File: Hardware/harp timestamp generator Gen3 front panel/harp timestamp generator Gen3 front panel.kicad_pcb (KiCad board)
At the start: 2 copper layers, 133 x 35 mm, 12 parts

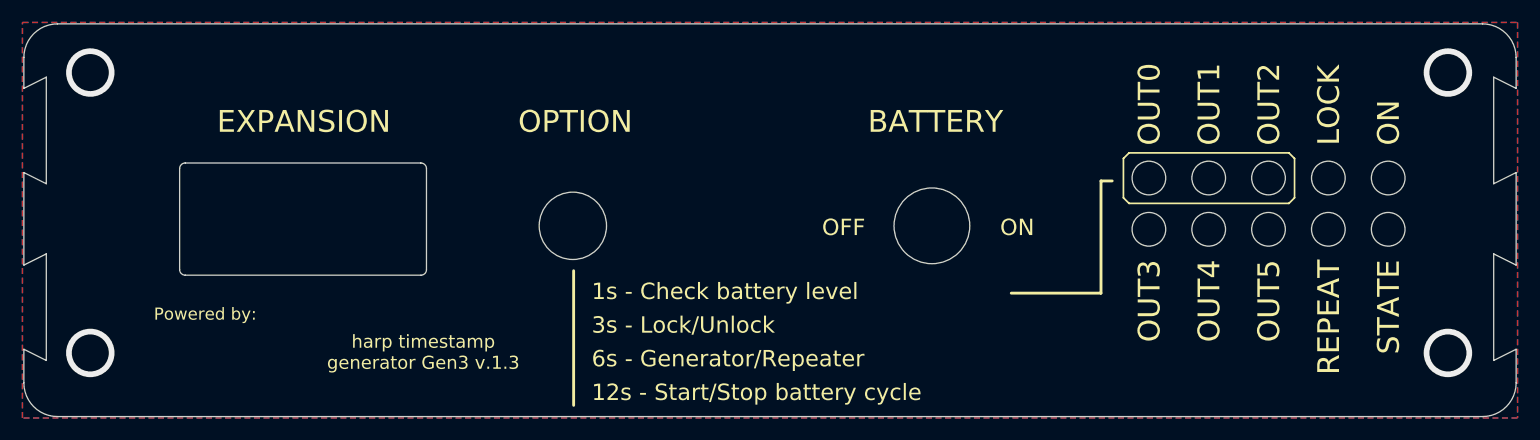
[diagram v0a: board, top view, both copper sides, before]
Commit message: ajuste posição ficha USB-C
> ajuste posição ficha USB-C
. actualizados manufacturing files:
   Gerbers & Drills & .d356 & P&P
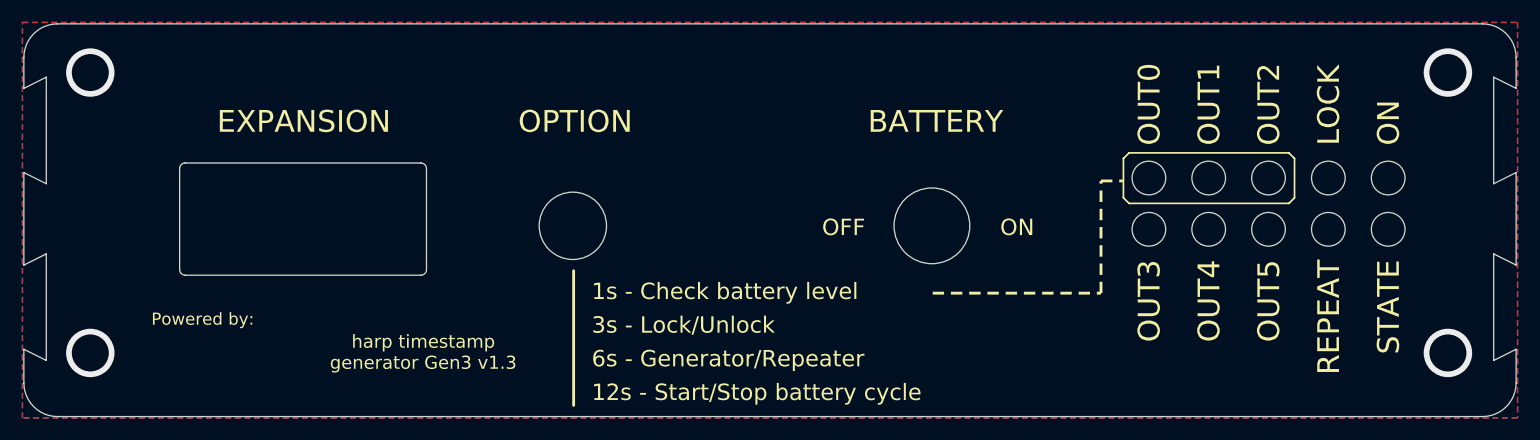
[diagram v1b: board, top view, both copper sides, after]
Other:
- board text added: "harp timestamp generator Gen3 v1.3"
- board text removed: "harp timestamp generator Gen3 v.1.3"
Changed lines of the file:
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@@
 			(usegerberattributes yes)
 			(usegerberadvancedattributes yes)
-			(creategerberjobfile yes)
+			(creategerberjobfile no)
 			(dashed_line_dash_ratio 12)
 			(dashed_line_gap_ratio 3)
@@
 			(plotframeref no)
 			(mode 1)
-			(useauxorigin no)
+			(useauxorigin yes)
 			(pdf_front_fp_property_popups yes)
 			(pdf_back_fp_property_popups yes)
@@
 			(sketchdnponfab yes)
 			(crossoutdnponfab yes)
-			(subtractmaskfromsilk no)
+			(subtractmaskfromsilk yes)
 			(outputformat 1)
 			(mirror no)
-			(drillshape 1)
+			(drillshape 0)
 			(scaleselection 1)
-			(outputdirectory "")
+			(outputdirectory "manufacturing/gerbers/")
 		)
 	)
@@
 	)
 	(gr_line
-		(start 170.0011 111.5036)
+		(start 163.0011 111.5036)
 		(end 178.0011 111.5036)
 		(stroke
 			(width 0.254)
-			(type solid)
+			(type dash)
 		)
 		(layer "F.SilkS")
@@
 	(gr_line
 		(start 178.0011 101.5036)
-		(end 179.0011 101.5036)
+		(end 179.95 101.5036)
 		(stroke
 			(width 0.254)
-			(type solid)
+			(type dash)
 		)
 		(layer "F.SilkS")
@@
 		(stroke
 			(width 0.254)
-			(type solid)
+			(type dash)
 		)
 		(layer "F.SilkS")
@@
 	)
 	(gr_text "Powered by:"
-		(at 93.583212 113.998894 0)
+		(at 93.36 114.45 0)
 		(layer "F.SilkS")
 		(effects
@@
 		)
 	)
-	(gr_text "harp timestamp\ngenerator Gen3 v.1.3"
+	(gr_text "harp timestamp\ngenerator Gen3 v1.3"
 		(at 117.6011 118.3908 0)
 		(layer "F.SilkS")
